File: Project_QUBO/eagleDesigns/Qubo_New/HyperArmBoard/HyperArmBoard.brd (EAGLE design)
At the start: 96.8 x 88.9 mm, 16 parts, among them U1 BME280

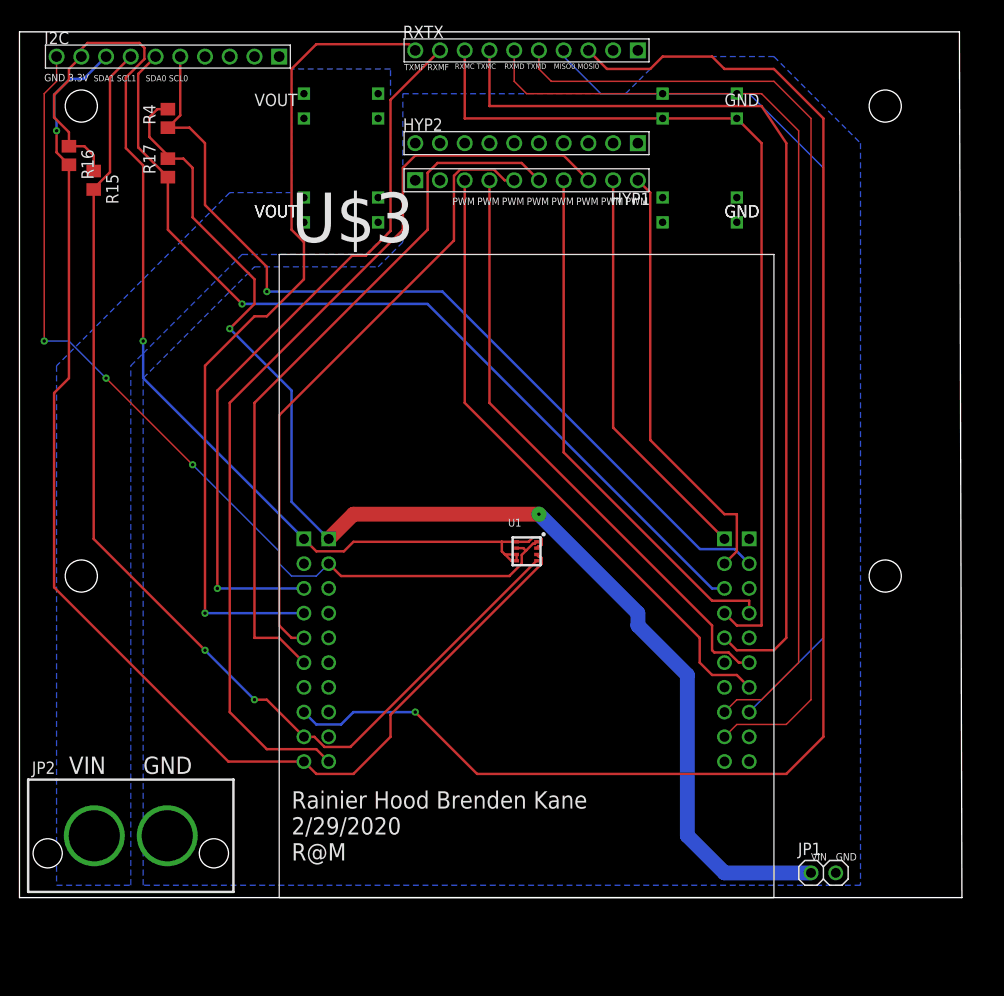
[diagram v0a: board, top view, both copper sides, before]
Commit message: made hyperarmboard
made newboard thatcombindes the hypertonics and arm board
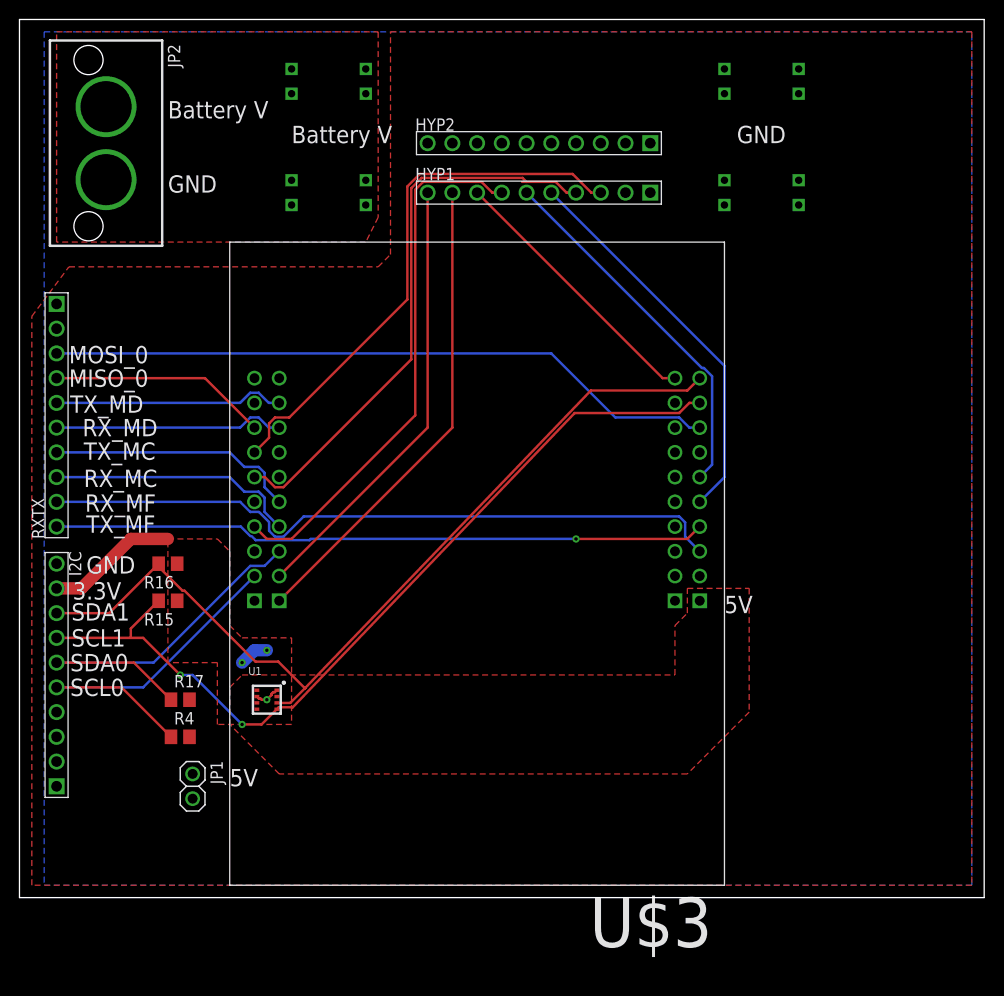
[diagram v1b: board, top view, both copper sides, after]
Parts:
- moved JP2 71.2 mm to (8.89, 77.5), turned to 270 degrees
- moved JP1 65.4 mm to (17.8, 11.4), turned to 270 degrees
- moved I2C 64.5 mm to (3.81, 22.9), turned to 270 degrees
- moved R4 63.5 mm to (16.5, 16.5), turned to 0 degrees
- moved RXTX 61.1 mm to (3.81, 49.5), turned to 90 degrees
- moved R17 54.6 mm to (16.5, 20.3), turned to 0 degrees
- moved R15 43.8 mm to (15.2, 30.5), turned to 180 degrees
- moved R16 43.1 mm to (15.2, 34.3), turned to 180 degrees
- moved U1 30.7 mm to (25.4, 20.3)
- moved U$6 14.7 mm to (76.2, 83.8)
- moved U$5 13.3 mm to (31.8, 83.8)
- moved U$7 10.9 mm to (76.2, 72.4)
- moved U$4 8.98 mm to (31.8, 72.4), turned to 90 degrees
- moved U$3 5.24 mm to (47.0, 34.3), turned to 180 degrees
- moved HYP1 1.80 mm to (53.3, 72.4), turned to 0 degrees
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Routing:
- net 5V: track 132.5 -> 0.00 mm, vias 2 -> 0
- net 3.3V: track 113.6 -> 16.6 mm, vias 1 -> 2
- net DGND: track 95.1 -> 2.66 mm, vias 3 -> 1
- net MOSI_0: track 150.2 -> 69.2 mm, vias 1 -> 0
- net TX_MD: track 102.1 -> 23.7 mm
- net RX_MD: track 98.8 -> 23.7 mm
- net TX_MC: track 96.4 -> 25.8 mm
- net MISO_0: track 91.1 -> 22.4 mm
- net PWM5: track 96.1 -> 28.2 mm
- net RX_MC: track 92.4 -> 25.8 mm
- net SCL_0: track 91.3 -> 38.9 mm, vias 1 -> 0
- net SDA_0: track 92.2 -> 40.9 mm, vias 1 -> 0
- net SDA_1: track 128.3 -> 90.7 mm, vias 1 -> 0
- net PWM3: track 73.8 -> 37.7 mm
- net SCL_1: track 113.3 -> 88.8 mm
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- added copper zone on layer 1, net 3.3V
- added copper zone on layer 1, net 5V
- added copper zone on layer 1, net BIGVIN
- removed copper zone on layer 16, net BIGVIN
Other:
- board size 96.8 x 88.9 mm -> 99.1 x 90.2 mm
- board text added: "3.3V"
- board text added: "5V"
- board text added: "Battery V"
- board text added: "MISO_0"
- board text added: "MOSI_0"
- board text added: "RX_MC"
- board text added: "RX_MD"
- board text added: "RX_MF"
- board text added: "SCL0"
- board text added: "SCL1"
- board text added: "SDA0"
- board text added: "SDA1"
- board text added: "TX_MC"
- board text added: "TX_MD"
- board text added: "TX_MF"
- board text removed: "GND 3.3V"
- board text removed: "MISO0 MOSI0"
- board text removed: "PWM"
- board text removed: "RXMC TXMC"
- board text removed: "RXMD TXMD"
- board text removed: "Rainier Hood Brenden Kane 2/29/2020 R@M"
- board text removed: "SDA0 SCL0"
- board text removed: "SDA1 SCL1"
- board text removed: "TXMF RXMF"
- board text removed: "VIN"
- board text removed: "VOUT"

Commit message: changes to hyperarm and power board
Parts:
- moved JP1 14.9 mm to (3.81, 6.35)
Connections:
- net RX_MF: no longer RXTX.P$9
- net RX_SF: now also RXTX.P$9
- net TX_MF: no longer RXTX.P$10
- net TX_SF: now also RXTX.P$10
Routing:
- net RX_MF: track 71.3 -> 0.00 mm
- net TX_MF: track 67.2 -> 0.00 mm, vias 1 -> 0
- net TX_SF: track 0.00 -> 27.1 mm, vias 0 -> 2
- net RX_SF: track 0.00 -> 25.0 mm
- net PWM0: track 55.9 -> 56.6 mm
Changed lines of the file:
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@@
 <text x="27.94" y="77.47" size="1.778" layer="21">Battery V</text>
 <text x="72.39" y="29.21" size="1.778" layer="21">5V</text>
-<text x="21.59" y="11.43" size="1.778" layer="21">5V</text>
+<text x="5.588" y="7.493" size="1.778" layer="21">5V</text>
 <text x="5.334" y="28.448" size="1.778" layer="21">SDA1</text>
 <text x="5.207" y="23.241" size="1.778" layer="21">SDA0</text>
@@
 <text x="5.08" y="52.451" size="1.778" layer="21">MISO_0</text>
 <text x="5.08" y="54.864" size="1.778" layer="21">MOSI_0</text>
+<text x="5.461" y="4.064" size="1.778" layer="112">GND</text>
 </plain>
 <attributes>
@@
 <element name="HYP2" library="molex" package="KK254_10-PIN" value="KK254_10-PIN" x="53.34" y="77.47"/>
 <element name="I2C" library="molex" package="KK254_10-PIN" value="KK254_10-PIN" x="3.81" y="22.86" rot="R270"/>
-<element name="JP1" library="pinhead" package="1X02" value="" x="17.78" y="11.43" rot="R270"/>
+<element name="JP1" library="pinhead" package="1X02" value="" x="3.81" y="6.35" rot="R270"/>
 <element name="JP2" library="molex" package="SUPERSABRE_2CIRCUIT" value="PWR" x="8.89" y="77.47" rot="R270"/>
 <element name="R15" library="resistor" library_urn="urn:adsk.eagle:library:348" package="R0805" package3d_urn="urn:adsk.eagle:package:26059/1" value="5k" x="15.24" y="30.48" rot="R180"/>
@@
 <signal name="RX_MF">
 <contactref element="U$3" pad="1-3"/>
-<contactref element="RXTX" pad="P$9"/>
-<wire x1="25.6286" y1="37.6686375" x2="26.2386375" y2="37.0586" width="0.254" layer="16"/>
-<wire x1="26.2386375" y1="37.0586" x2="27.1013625" y2="37.0586" width="0.254" layer="16"/>
-<wire x1="67.7413625" y1="39.1414" x2="68.3514" y2="38.5313625" width="0.254" layer="16"/>
-<wire x1="3.81" y1="40.64" x2="22.6572375" y2="40.64" width="0.254" layer="16"/>
-<wire x1="23.6986375" y1="39.5986" x2="24.5966625" y2="39.5986" width="0.254" layer="16"/>
-<wire x1="68.3514" y1="37.0586" x2="69.85" y2="35.56" width="0.254" layer="16"/>
-<wire x1="22.6572375" y1="40.64" x2="23.6986375" y2="39.5986" width="0.254" layer="16"/>
-<wire x1="24.5966625" y1="39.5986" x2="25.6286" y2="38.5666625" width="0.254" layer="16"/>
-<wire x1="25.6286" y1="38.5666625" x2="25.6286" y2="37.6686375" width="0.254" layer="16"/>
-<wire x1="68.3514" y1="38.5313625" x2="68.3514" y2="37.0586" width="0.254" layer="16"/>
-<wire x1="29.1841625" y1="39.1414" x2="67.7413625" y2="39.1414" width="0.254" layer="16"/>
-<wire x1="27.1013625" y1="37.0586" x2="29.1841625" y2="39.1414" width="0.254" layer="16"/>
 </signal>
 <signal name="TX_MF">
 <contactref element="U$3" pad="1-4"/>
-<contactref element="RXTX" pad="P$10"/>
-<wire x1="23.719675" y1="37.1094" x2="23.8506" y2="37.1094" width="0.1524" layer="16"/>
-<wire x1="3.81" y1="38.1" x2="22.729075" y2="38.1" width="0.254" layer="16"/>
-<wire x1="22.729075" y1="38.1" x2="23.719675" y2="37.1094" width="0.254" layer="16"/>
-<wire x1="29.7886625" y1="36.703" x2="29.9156625" y2="36.83" width="0.254" layer="16"/>
-<wire x1="23.8506" y1="37.1094" x2="24.257" y2="36.703" width="0.254" layer="16"/>
-<wire x1="24.257" y1="36.703" x2="29.7886625" y2="36.703" width="0.254" layer="16"/>
-<wire x1="29.9156625" y1="36.83" x2="57.15" y2="36.83" width="0.254" layer="16"/>
-<via x="57.15" y="36.83" extent="1-16" drill="0.35"/>
-<wire x1="57.15" y1="36.83" x2="68.58" y2="36.83" width="0.254" layer="1"/>
-<wire x1="68.58" y1="36.83" x2="69.85" y2="38.1" width="0.254" layer="1"/>
 </signal>
 <signal name="3.3V">
@@
 <polygon width="0.254" layer="16">
 <vertex x="2.54" y="88.9"/>
-<vertex x="2.54" y="1.27"/>
+<vertex x="1.27" y="-1.27"/>
 <vertex x="97.79" y="1.27"/>
 <vertex x="97.79" y="88.9"/>
@@
 <signal name="RX_SF">
 <contactref element="U$3" pad="4-6"/>
+<contactref element="RXTX" pad="P$9"/>
+<wire x1="3.81" y1="40.64" x2="19.05" y2="40.64" width="0.254" layer="1"/>
+<wire x1="19.05" y1="40.64" x2="22.86" y2="44.45" width="0.254" layer="1"/>
+<wire x1="22.86" y1="44.45" x2="25.4" y2="44.45" width="0.254" layer="1"/>
+<wire x1="25.4" y1="44.45" x2="26.67" y2="43.18" width="0.254" layer="1"/>
 </signal>
 <signal name="TX_SF">
 <contactref element="U$3" pad="4-7"/>
+<contactref element="RXTX" pad="P$10"/>
+<wire x1="3.81" y1="38.1" x2="7.62" y2="38.1" width="0.254" layer="16"/>
+<wire x1="7.62" y1="38.1" x2="11.43" y2="41.91" width="0.254" layer="16"/>
+<via x="11.43" y="41.91" extent="1-16" drill="0.35"/>
+<wire x1="11.43" y1="41.91" x2="16.51" y2="46.99" width="0.254" layer="1"/>
+<wire x1="16.51" y1="46.99" x2="20.32" y2="46.99" width="0.254" layer="1"/>
+<via x="20.32" y="46.99" extent="1-16" drill="0.35"/>
+<wire x1="20.32" y1="46.99" x2="25.4" y2="46.99" width="0.254" layer="16"/>
+<wire x1="25.4" y1="46.99" x2="26.67" y2="45.72" width="0.254" layer="16"/>
 </signal>
 <signal name="RX_MD">
@@
 <contactref element="I2C" pad="P$7"/>
 <wire x1="26.425" y1="19.345" x2="26.6206" y2="19.5406" width="0.254" layer="1"/>
-<wire x1="26.6206" y1="19.5406" x2="28.06073125" y2="19.5406" width="0.254" layer="1"/>
+<wire x1="26.6206" y1="19.5406" x2="29.33073125" y2="19.5406" width="0.254" layer="1"/>
 <wire x1="68.7827625" y1="50.8" x2="69.85" y2="50.8" width="0.254" layer="1"/>
 <wire x1="67.7413625" y1="49.7586" x2="68.7827625" y2="50.8" width="0.254" layer="1"/>
-<wire x1="28.06073125" y1="19.5406" x2="57.00873125" y2="49.7586" width="0.254" layer="1"/>
-<wire x1="57.00873125" y1="49.7586" x2="67.7413625" y2="49.7586" width="0.254" layer="1"/>
+<wire x1="29.33073125" y1="19.5406" x2="55.74780625" y2="47.1166375" width="0.254" layer="1"/>
+<wire x1="55.74780625" y1="47.1166375" x2="58.27873125" y2="49.7586" width="0.254" layer="1"/>
+<wire x1="58.27873125" y1="49.7586" x2="67.7413625" y2="49.7586" width="0.254" layer="1"/>
 <wire x1="26.425" y1="19.345" x2="24.86" y2="17.78" width="0.254" layer="1"/>
 <via x="22.86" y="17.78" extent="1-16" drill="0.35"/>
@@
 <contactref element="HYP1" pad="P$4"/>
 <wire x1="27.1013625" y1="42.1386" x2="26.2386375" y2="42.1386" width="0.254" layer="1"/>
-<wire x1="40.2336" y1="72.8502" x2="41.2842" y2="73.9008" width="0.254" layer="1"/>
+<wire x1="39.8526" y1="72.7232" x2="41.2842" y2="74.2818" width="0.254" layer="1"/>
 <wire x1="25.1972375" y1="43.18" x2="24.13" y2="43.18" width="0.254" layer="1"/>
 <wire x1="26.2386375" y1="42.1386" x2="25.1972375" y2="43.18" width="0.254" layer="1"/>
-<wire x1="57.15" y1="72.39" x2="56.1718625" y2="72.39" width="0.254" layer="1"/>
-<wire x1="56.1718625" y1="72.39" x2="55.0674625" y2="73.4944" width="0.254" layer="1"/>
-<wire x1="40.2336" y1="72.8502" x2="40.2336" y2="55.2708375" width="0.254" layer="1"/>
-<wire x1="40.2336" y1="55.2708375" x2="27.1013625" y2="42.1386" width="0.254" layer="1"/>
-<wire x1="55.0674625" y1="73.4944" x2="52.07" y2="73.4944" width="0.254" layer="1"/>
-<wire x1="52.07" y1="73.4944" x2="51.6125375" y2="73.4944" width="0.254" layer="1"/>
-<wire x1="51.6636" y1="73.9008" x2="52.07" y2="73.4944" width="0.254" layer="1"/>
-<wire x1="41.2842" y1="73.9008" x2="51.6636" y2="73.9008" width="0.254" layer="1"/>
+<wire x1="39.8526" y1="72.7232" x2="39.8526" y2="55.1438375" width="0.254" layer="1"/>
+<wire x1="39.8526" y1="55.1438375" x2="27.1013625" y2="42.1386" width="0.254" layer="1"/>
+<wire x1="55.2582" y1="74.2818" x2="57.15" y2="72.39" width="0.254" layer="1"/>
+<wire x1="41.2842" y1="74.2818" x2="55.2582" y2="74.2818" width="0.254" layer="1"/>
 </signal>
 <signal name="PWM0">
 <contactref element="U$3" pad="2-7"/>
 <contactref element="HYP1" pad="P$3"/>
-<wire x1="39.8272" y1="73.0185375" x2="39.8272" y2="61.4172" width="0.254" layer="1"/>
+<wire x1="39.0652" y1="61.4172" x2="39.0652" y2="73.0185375" width="0.254" layer="1"/>
 <wire x1="26.2386375" y1="49.3014" x2="25.6286" y2="48.6913625" width="0.254" layer="1"/>
-<wire x1="41.1158625" y1="74.3072" x2="39.8272" y2="73.0185375" width="0.254" layer="1"/>
-<wire x1="59.69" y1="72.39" x2="58.7118625" y2="72.39" width="0.254" layer="1"/>
-<wire x1="39.8272" y1="61.4172" x2="27.7114" y2="49.3014" width="0.254" layer="1"/>
+<wire x1="39.0652" y1="61.4172" x2="27.7114" y2="49.3014" width="0.254" layer="1"/>
 <wire x1="25.6286" y1="47.2186" x2="24.13" y2="45.72" width="0.254" layer="1"/>
 <wire x1="27.7114" y1="49.3014" x2="26.2386375" y2="49.3014" width="0.254" layer="1"/>
 <wire x1="25.6286" y1="48.6913625" x2="25.6286" y2="47.2186" width="0.254" layer="1"/>
-<wire x1="58.7118625" y1="72.39" x2="56.7946625" y2="74.3072" width="0.254" layer="1"/>
-<wire x1="56.7946625" y1="74.3072" x2="41.1158625" y2="74.3072" width="0.254" layer="1"/>
+<wire x1="39.0652" y1="73.0185375" x2="40.9766625" y2="74.93" width="0.254" layer="1"/>
+<wire x1="57.15" y1="74.93" x2="59.69" y2="72.39" width="0.254" layer="1"/>
+<wire x1="40.9766625" y1="74.93" x2="57.15" y2="74.93" width="0.254" layer="1"/>
 </signal>
 <signal name="PWM5">
@@
 </signal>
 </signals>
+<errors>
+</errors>
 </board>
 </drawing>
